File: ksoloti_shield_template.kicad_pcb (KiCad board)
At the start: 4 copper layers, 120 x 100 mm, 101 parts, among them J1_P1 IN_L, J1_P2 IN_GND, J1_P3 IN_R, J1_P4 OUT_R, J1_P5 OUT_GND, J1_P6 OUT_L, J2_P1 HP_R, J2_P2 HP_GND, J2_P3 HP_L, J8_P1 GND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

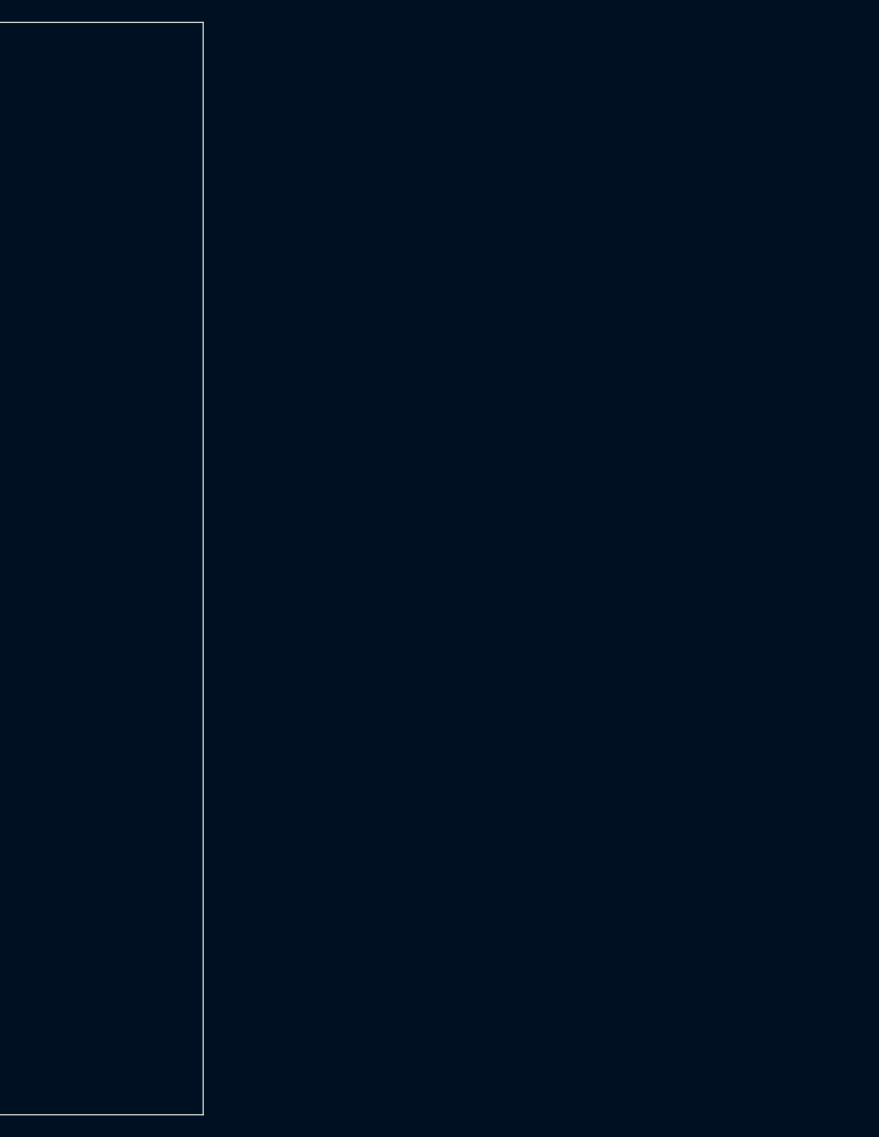
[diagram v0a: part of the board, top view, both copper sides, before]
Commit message: add a selection of symbols and footprints to start out with: pots, switches, encoder, jacks, LEDs,  OLED ...
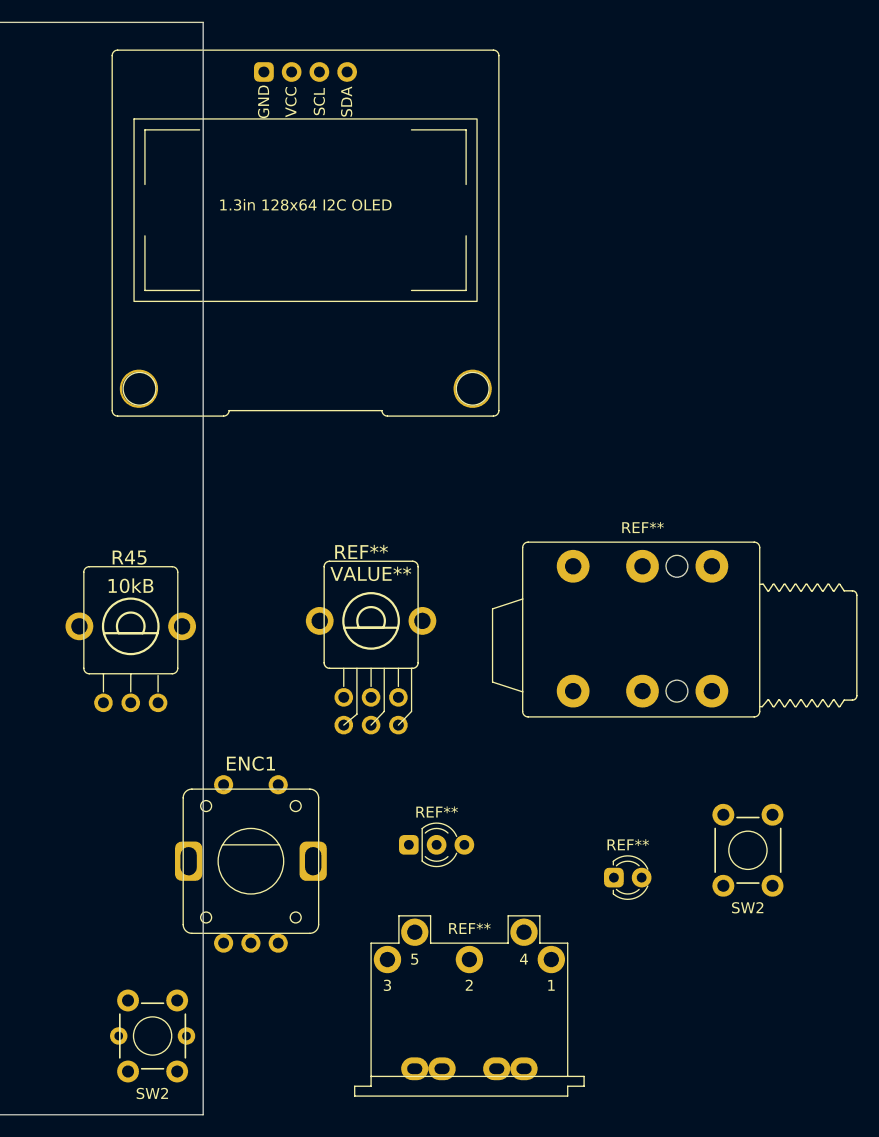
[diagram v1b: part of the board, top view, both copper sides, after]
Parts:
- added DIN-5: REF**, ksoloti_shield_footprints:MIDI_DIN-5_DS-5-01c, F.Cu at (233.0, 143.8)
- added ENC1: MENU_ENCODER, ksoloti_shield_footprints:ALPS_STEC12E08, F.Cu at (213.0, 122.3)
- added OLED1: 128x64_OLED, ksoloti_shield_footprints:128x64OLED_1_3in, F.Cu at (218.0, 64.8)
- added R45: 10kB, ksoloti_shield_footprints:ALPS_POT_VERTICAL_PS, F.Cu at (202.0, 100.8)
- added REF**: LED_D3.0mm-3_marked, ksoloti_shield_footprints:LED_D3.0mm-3_marked, F.Cu at (230.0, 120.8)
- added REF**: VALUE**, ksoloti_shield_footprints:ALPS_POT_VERTICAL_PS_DUAL, F.Cu at (224.0, 100.3)
- added REF**: LED_D3.0mm_marked, ksoloti_shield_footprints:LED_D3.0mm_marked, F.Cu at (247.5, 123.8)
- added REF**: Jack_6.35mm_Neutrik_NRJ6HF_Horizontal_no_screwhole, ksoloti_shield_footprints:Jack_6.35mm_Neutrik_NRJ6HF_Horizontal_no_screwhole, F.Cu at (242.5, 95.3)
- added SW2: TAC_SWITCHPTH, ksoloti_shield_footprints:TL1105T, F.Cu at (258.5, 121.3)
- added SW2: TAC_SWITCHPTH, ksoloti_shield_footprints:TL1105T_with_LED, F.Cu at (204.0, 138.3)

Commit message: fix accidental placement of random footprints
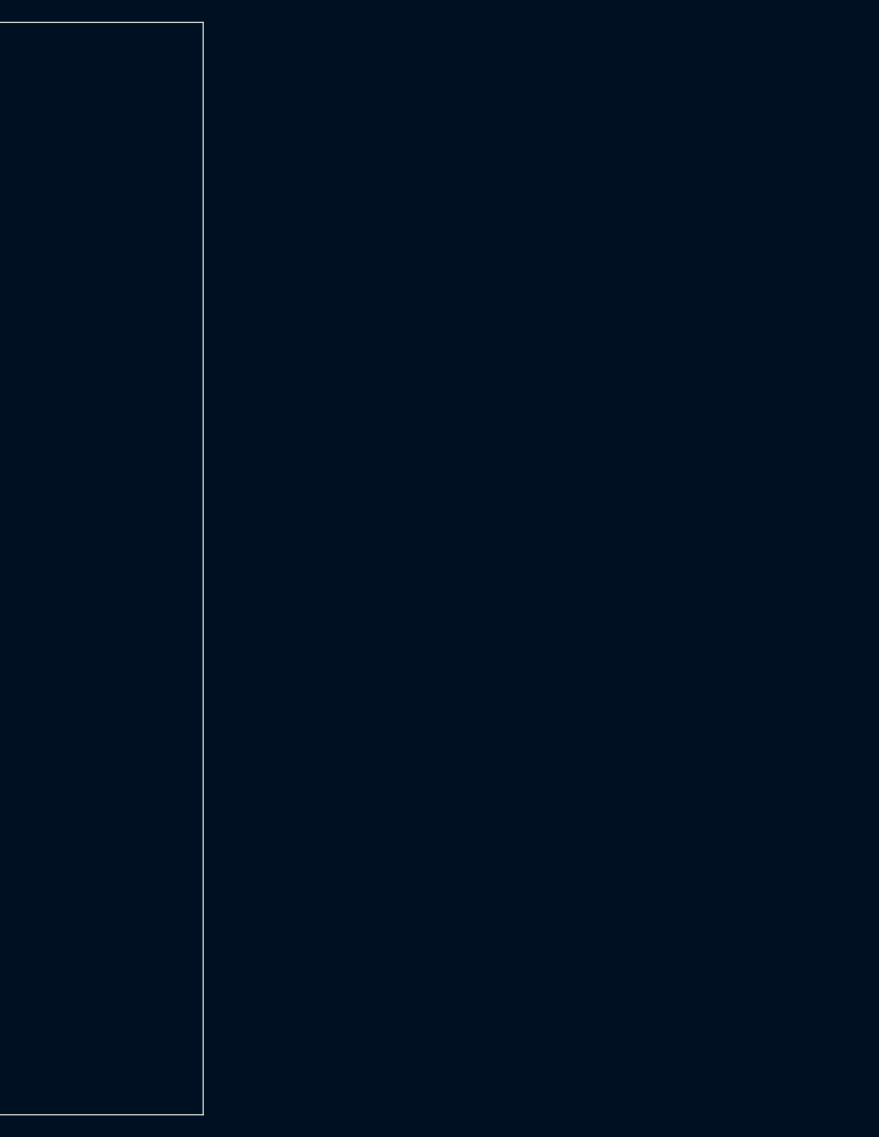
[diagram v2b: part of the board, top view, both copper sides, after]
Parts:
- removed DIN-5: REF**, ksoloti_shield_footprints:MIDI_DIN-5_DS-5-01c
- removed ENC1: MENU_ENCODER, ksoloti_shield_footprints:ALPS_STEC12E08
- removed OLED1: 128x64_OLED, ksoloti_shield_footprints:128x64OLED_1_3in
- removed R45: 10kB, ksoloti_shield_footprints:ALPS_POT_VERTICAL_PS
- removed REF**: LED_D3.0mm-3_marked, ksoloti_shield_footprints:LED_D3.0mm-3_marked
- removed REF**: VALUE**, ksoloti_shield_footprints:ALPS_POT_VERTICAL_PS_DUAL
- removed REF**: LED_D3.0mm_marked, ksoloti_shield_footprints:LED_D3.0mm_marked
- removed REF**: Jack_6.35mm_Neutrik_NRJ6HF_Horizontal_no_screwhole, ksoloti_shield_footprints:Jack_6.35mm_Neutrik_NRJ6HF_Horizontal_no_screwhole
- removed SW2: TAC_SWITCHPTH, ksoloti_shield_footprints:TL1105T
- removed SW2: TAC_SWITCHPTH, ksoloti_shield_footprints:TL1105T_with_LED
